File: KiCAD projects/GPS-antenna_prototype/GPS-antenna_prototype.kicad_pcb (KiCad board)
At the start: 2 copper layers, 74.9 x 134.6 mm, 1 part, among them J1 MMCX_Connector

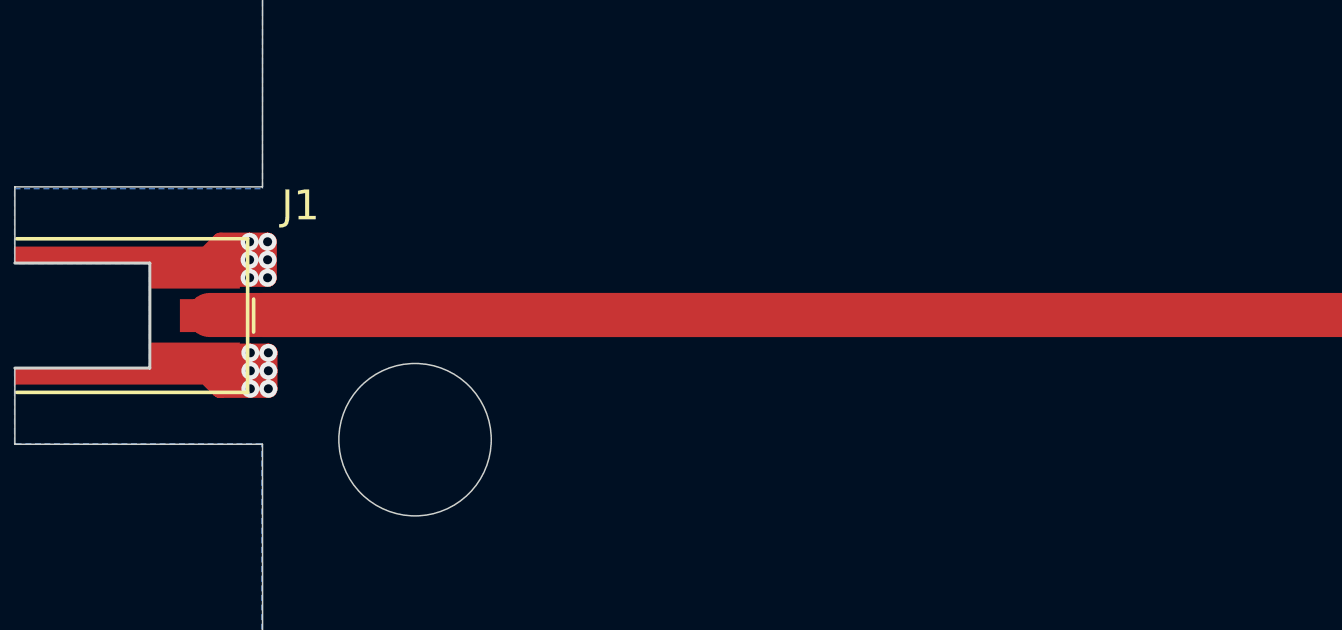
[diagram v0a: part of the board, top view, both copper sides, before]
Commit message: fixed clearance violation on GPS board and generated V4 fabrication outputs
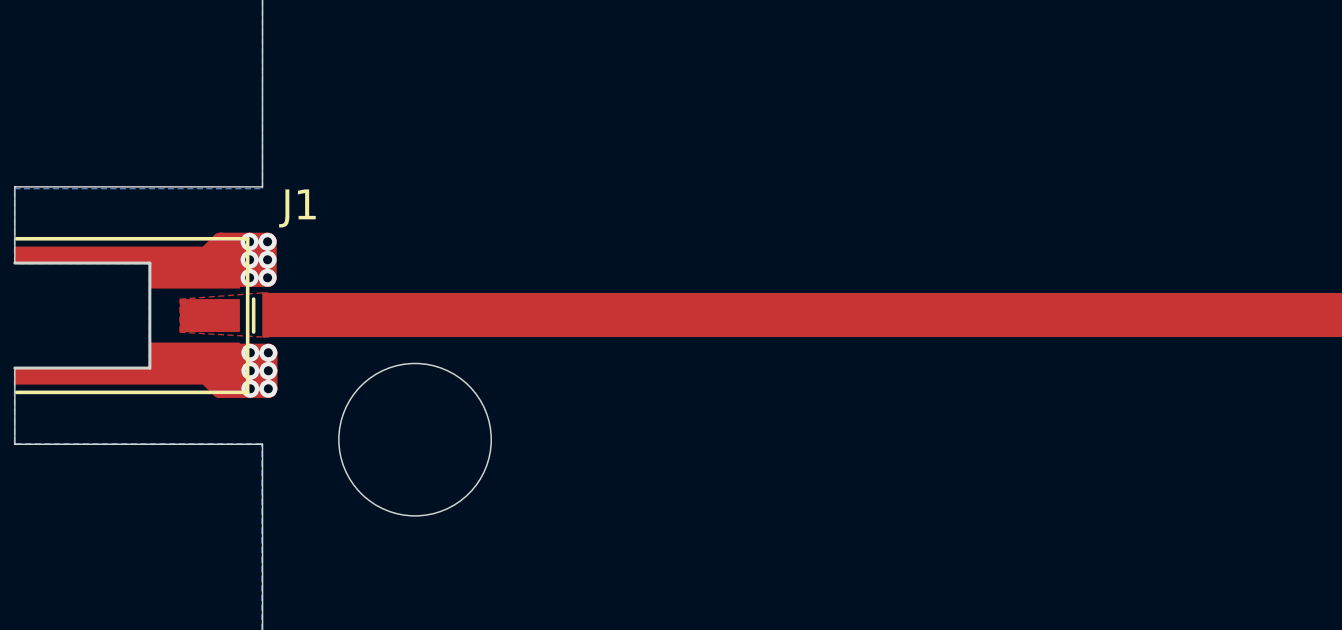
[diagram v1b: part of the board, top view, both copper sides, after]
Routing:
- net RadElement: track 31.0 -> 0.00 mm
- added copper zone on F.Cu, net RadElement
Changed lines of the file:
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@@
 			(keep_text_aligned yes)
 		)
-		(gr_text "275.5906"
+		(gr_text "7"
 			(at 79.52 61.4 90)
 			(layer "User.1")
@@
 			(keep_text_aligned yes)
 		)
-		(gr_text "1604.3307"
+		(gr_text "40.75"
 			(at 142.745 135.275 90)
 			(layer "User.1")
@@
 			(keep_text_aligned yes)
 		)
-		(gr_text "472.4409"
+		(gr_text "12"
 			(at 115.295 124.1 90)
 			(layer "User.1")
@@
 			(keep_text_aligned yes)
 		)
-		(gr_text "1464.5669"
+		(gr_text "37.2"
 			(at 114.745 104.5 90)
 			(layer "User.1")
@@
 			(keep_text_aligned yes)
 		)
-		(gr_text "1889.7638"
+		(gr_text "48"
 			(at 120.545 63.1 0)
 			(layer "User.1")
@@
 			(keep_text_aligned yes)
 		)
-		(gr_text "2178.1496"
+		(gr_text "55.325"
 			(at 78.87 85.5625 90)
 			(layer "User.1")
@@
 			(keep_text_aligned yes)
 		)
-		(gr_text "1968.5039"
+		(gr_text "50"
 			(at 142.745 89.9 90)
 			(layer "User.1")
@@
 			(keep_text_aligned yes)
 		)
-		(gr_text "787.4016"
+		(gr_text "20"
 			(at 107.095 56.1 0)
 			(layer "User.1")
@@
 			(keep_text_aligned yes)
 		)
-		(gr_text "157.4803"
+		(gr_text "4"
 			(at 119.095 116.3 0)
 			(layer "User.1")
@@
 			(keep_text_aligned yes)
 		)
-		(gr_text "905.5118"
+		(gr_text "23"
 			(at 115.295 69.4 90)
 			(layer "User.1")
@@
 			)
 		)
-	)
-	(segment
-		(start 89.033772 116.17635)
-		(end 120.043772 116.17635)
-		(width 1.47)
-		(layer "F.Cu")
-		(net "RadElement")
 	)
 	(segment
@@
 	)
 	(zone
+		(net "RadElement")
+		(layer "F.Cu")
+		(hatch edge 0.5)
+		(priority 1)
+		(connect_pads yes
+			(clearance 0)
+		)
+		(min_thickness 0.25)
+		(fill yes
+			(thermal_gap 0.5)
+			(thermal_bridge_width 0.5)
+			(island_removal_mode 0)
+		)
+		(polygon
+			(pts
+				(xy 88.05 115.65) (xy 90.793772 115.44135) (xy 91.021622 115.44135) (xy 91.021628 116.911349) (xy 90.793772 116.91135)
+				(xy 88.05 116.75)
+			)
+		)
+	)
+	(zone
